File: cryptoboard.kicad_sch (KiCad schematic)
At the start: 37 parts, among them J1 USB_A, J2 BOOT, J3 SWD, J4 USR_LEFT, J5 USR_RIGHT, J6 Conn_01x04, SW1 SW_Push, U1 STM32F103C8Tx, U2 LM317_SOT-223-3.3V, U3 STM32F107RBTx, Y1 Crystal

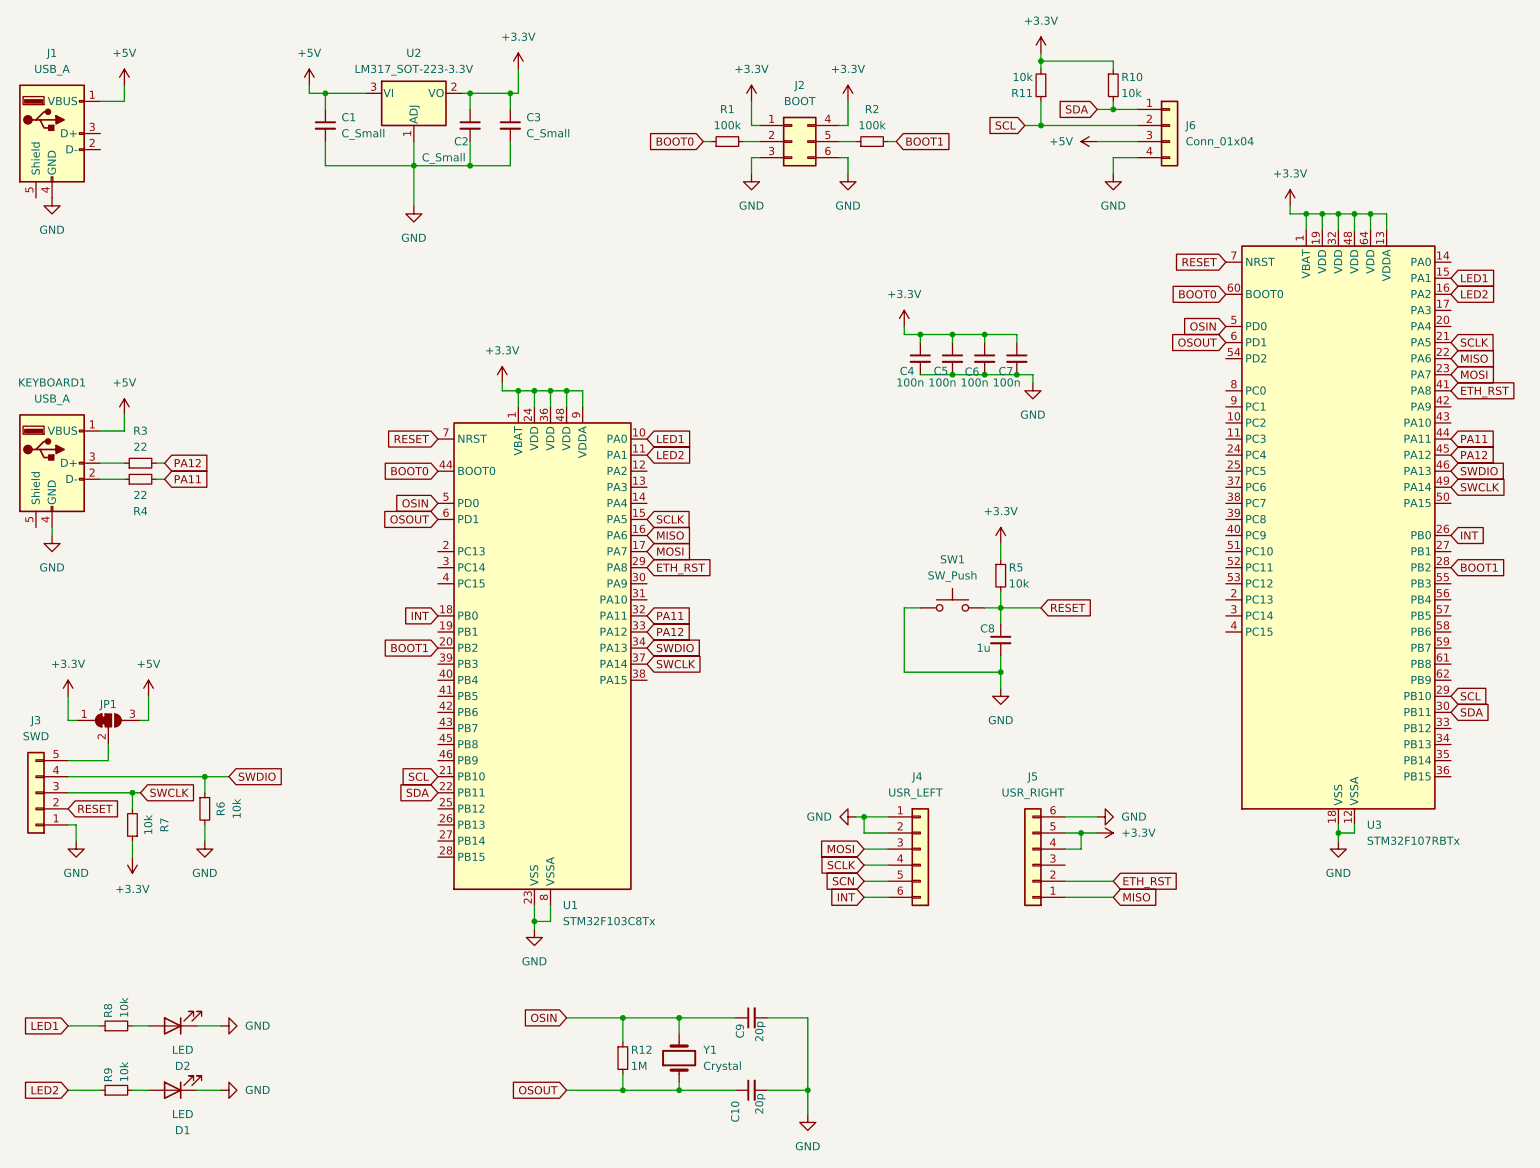
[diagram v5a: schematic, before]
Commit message: stm32f103 to stm32f107
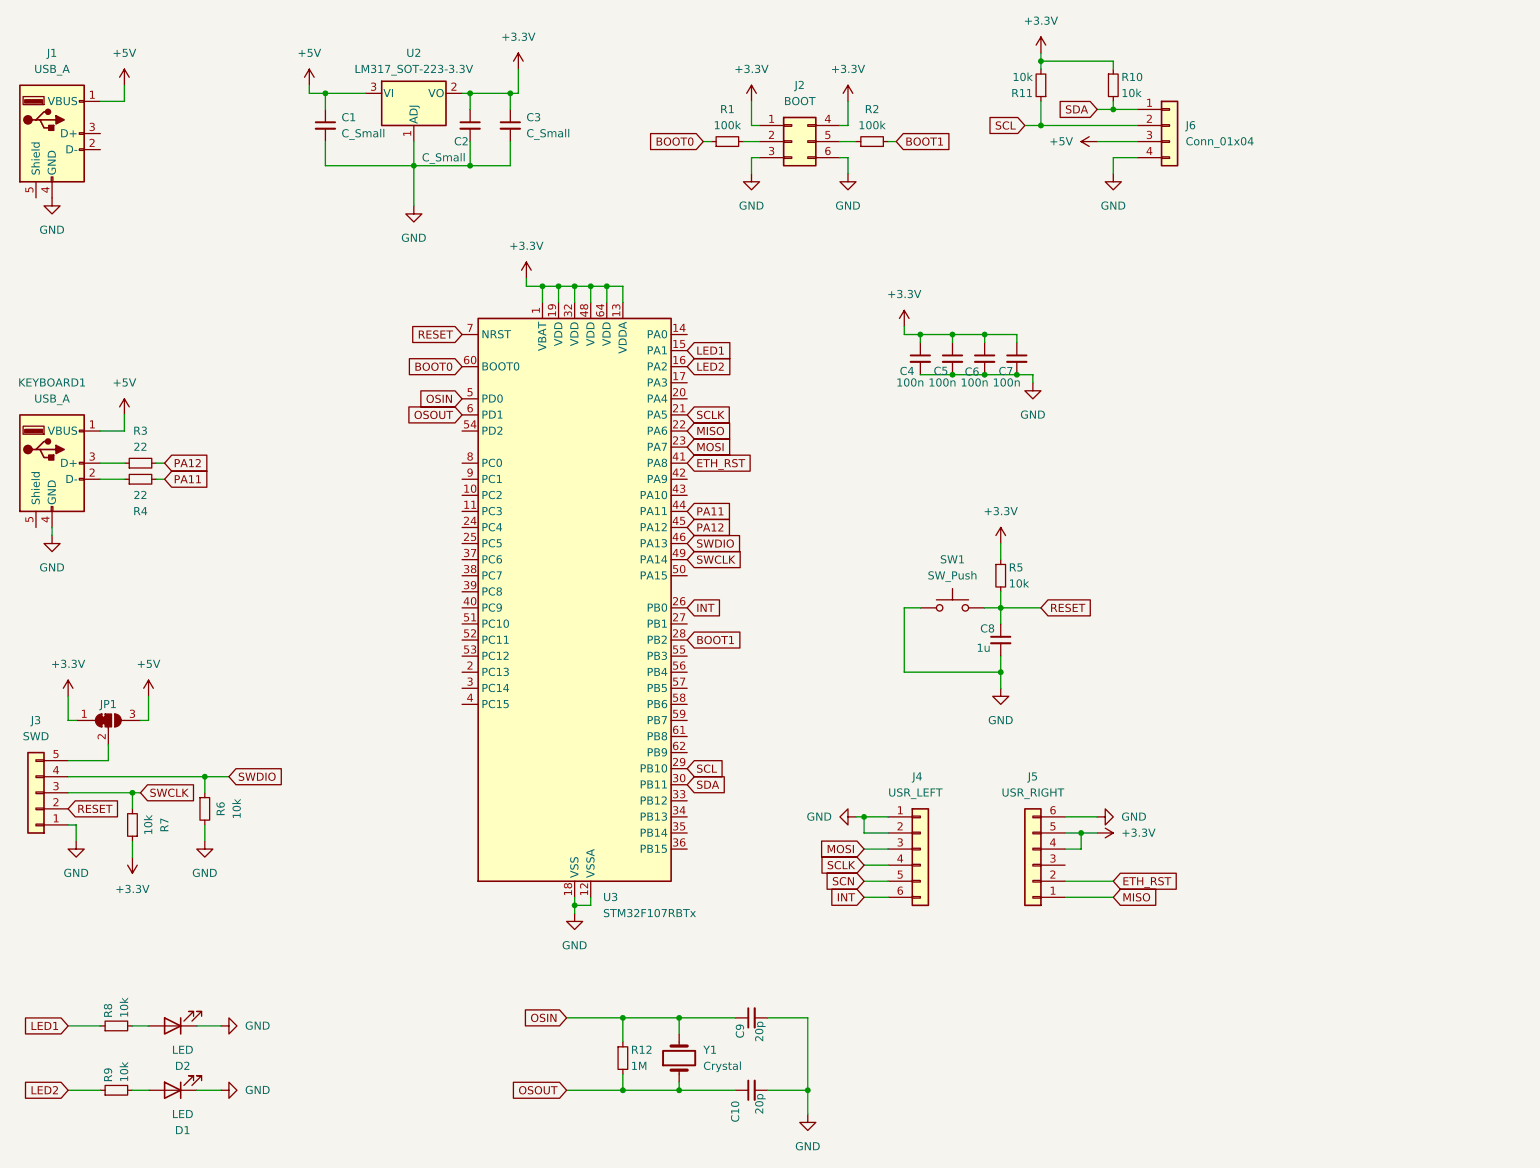
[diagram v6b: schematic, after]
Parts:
- removed U1: STM32F103C8Tx, Package_QFP:LQFP-48_7x7mm_P0.5mm, symbol MCU_ST_STM32F1:STM32F103C8Tx
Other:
- moved on the sheet: U3
